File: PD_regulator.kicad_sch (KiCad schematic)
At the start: 26 parts, among them J5 Switch, J6 Fast_Out, U5 ADA4896-2ARMZ, U8 ADG1413, U9 LTC6228xS8

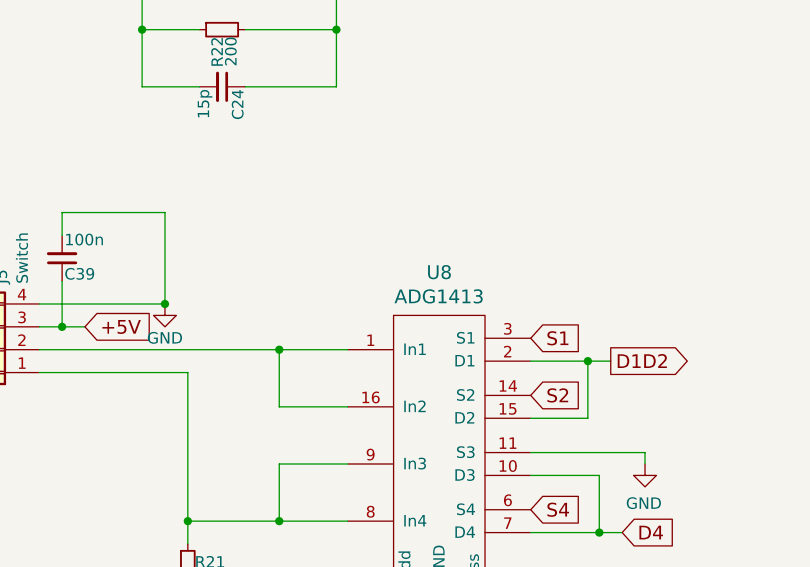
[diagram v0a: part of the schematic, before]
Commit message: Fix HMC365 and ADG1413 symbols. Update gerber files.
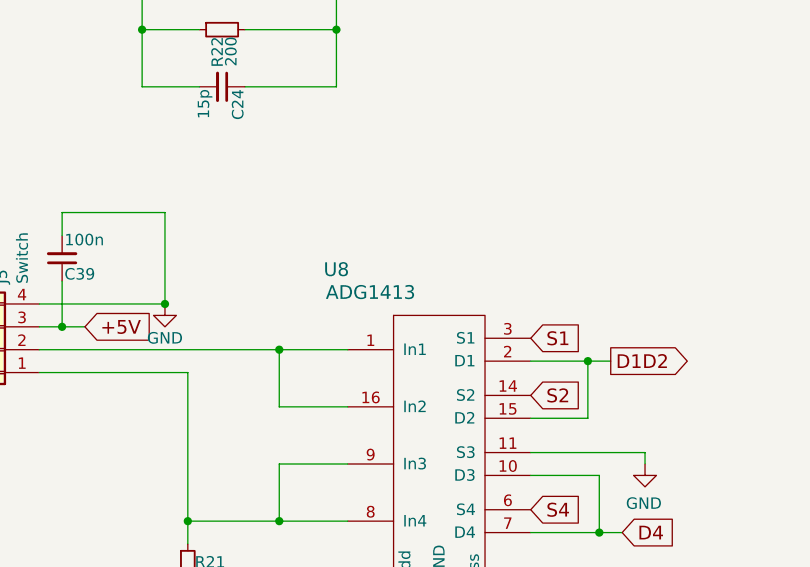
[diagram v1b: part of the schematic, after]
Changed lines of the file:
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@@
   (symbol (lib_id "Linear-Technology:ADG1413") (at 121.92 129.54 0) (unit 1)
     (in_bom yes) (on_board yes)
-    (property "Reference" "U8" (id 0) (at 121.92 104.4702 0)
+    (property "Reference" "U8" (id 0) (at 110.49 104.14 0)
       (effects (font (size 1.524 1.524)))
     )
-    (property "Value" "ADG1413" (id 1) (at 121.92 107.1626 0)
+    (property "Value" "ADG1413" (id 1) (at 114.3 106.68 0)
       (effects (font (size 1.524 1.524)))
     )
-    (property "Footprint" "Package_SO:TSSOP-16_4.4x5mm_P0.65mm" (id 2) (at 121.92 134.62 0)
+    (property "Footprint" "Package_SO:TSSOP-16_4.4x5mm_P0.65mm" (id 2) (at 154.94 142.24 0)
       (effects (font (size 1.524 1.524)) hide)
     )
@@
     (pin "10")
     (pin "11")
+    (pin "12")
     (pin "13")
     (pin "14")

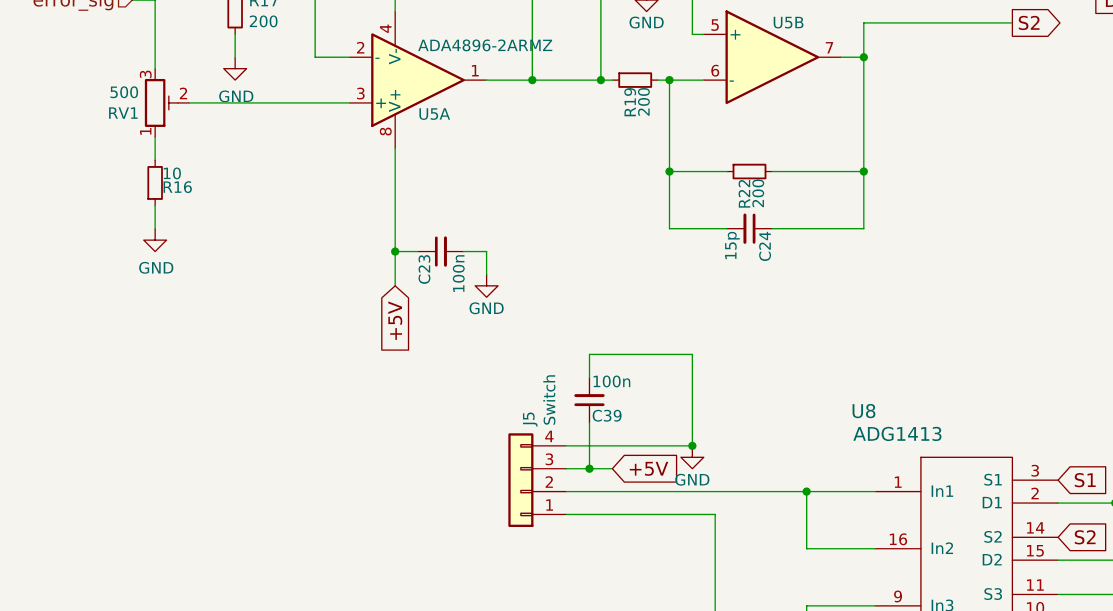
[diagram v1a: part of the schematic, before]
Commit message: Update BOM / fix some fottprints
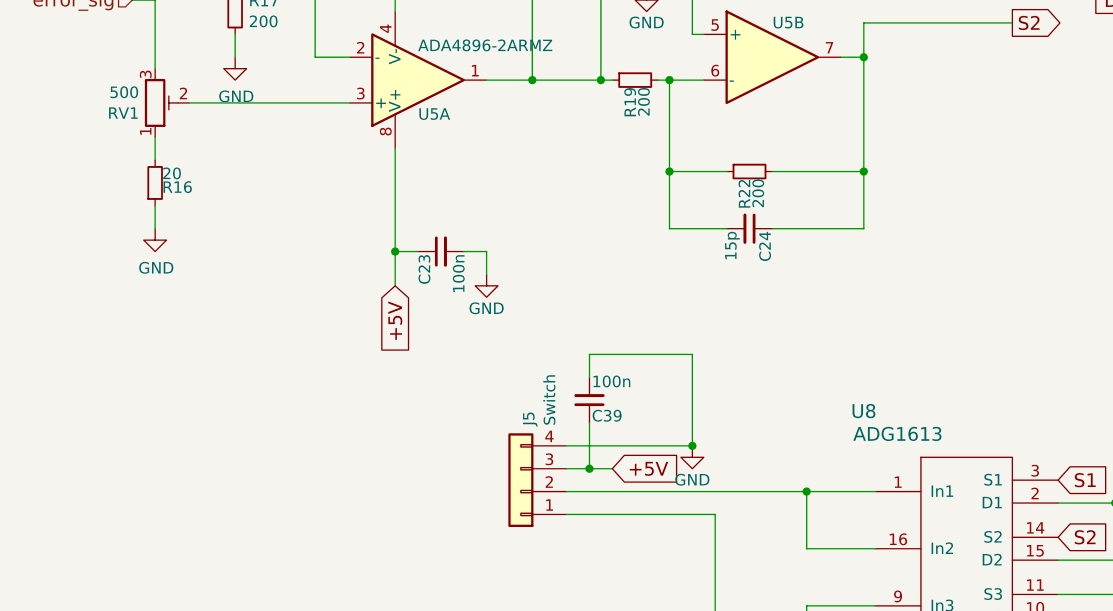
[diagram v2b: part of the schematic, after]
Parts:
- C38: Config (none) -> DNF
- R16: value 10 -> 20; MFN (none) -> Yageo; PN (none) -> AC0603FR-0720RL
- R17, R18: footprint Capacitor_SMD:C_0603_1608Metric -> Resistor_SMD:R_0603_1608Metric; MFN (none) -> Yageo; PN (none) -> RC0603FR-13200RL
- R19, R22, R23, R25: MFN (none) -> Yageo; PN (none) -> RC0603FR-13200RL
- U5: MFN (none) -> Analog Devices; PN (none) -> ADA4896-2ARMZ
- U8: value ADG1413 -> ADG1613; MFN (none) -> Analog Devices; PN (none) -> ADG1613BRUZ
- U9: MFN (none) -> Analog Devices; PN (none) -> LTC6228IS8#PBF
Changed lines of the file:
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@@
+      (effects (font (size 1.27 1.27)) hide)
+    )
+    (property "MFN" "Yageo" (id 4) (at 157.48 58.42 0)
+      (effects (font (size 1.27 1.27)) hide)
+    )
+    (property "PN" "RC0603FR-13200RL" (id 5) (at 157.48 58.42 0)
       (effects (font (size 1.27 1.27)) hide)
     )
@@
     )
     (property "Datasheet" "" (id 3) (at 191.77 26.67 0)
+      (effects (font (size 1.27 1.27)) hide)
+    )
+    (property "MFN" "Yageo" (id 4) (at 191.77 26.67 0)
+      (effects (font (size 1.27 1.27)) hide)
+    )
+    (property "PN" "RC0603FR-13200RL" (id 5) (at 191.77 26.67 0)
       (effects (font (size 1.27 1.27)) hide)
     )
@@
     (property "Datasheet" "https://www.analog.com/media/en/technical-documentation/data-sheets/LTC6228-6229.pdf" (id 3) (at 194.31 60.96 0)
       (effects (font (size 1.27 1.27)) hide)
+    )
+    (property "MFN" "Analog Devices" (id 4) (at 194.31 60.96 0)
+      (effects (font (size 1.524 1.524)) hide)
+    )
+    (property "PN" "LTC6228IS8#PBF" (id 5) (at 194.31 60.96 0)
+      (effects (font (size 1.524 1.524)) hide)
     )
     (pin "1")
@@
       (effects (font (size 1.524 1.524)))
     )
-    (property "Value" "ADG1413" (id 1) (at 114.3 106.68 0)
+    (property "Value" "ADG1613" (id 1) (at 114.3 106.68 0)
       (effects (font (size 1.524 1.524)))
     )
@@
     )
     (property "Datasheet" "" (id 3) (at 121.92 134.62 0)
+      (effects (font (size 1.524 1.524)) hide)
+    )
+    (property "MFN" "Analog Devices" (id 4) (at 121.92 129.54 0)
+      (effects (font (size 1.524 1.524)) hide)
+    )
+    (property "PN" "ADG1613BRUZ" (id 5) (at 121.92 129.54 0)
       (effects (font (size 1.524 1.524)) hide)
     )
@@
       (effects (font (size 1.27 1.27)) (justify left))
     )
-    (property "Footprint" "Capacitor_SMD:C_0603_1608Metric" (id 2) (at 40.64 59.69 0)
+    (property "Footprint" "Resistor_SMD:R_0603_1608Metric" (id 2) (at 40.64 59.69 0)
       (effects (font (size 1.27 1.27)) hide)
     )
     (property "Datasheet" "~" (id 3) (at 40.64 59.69 0)
+      (effects (font (size 1.27 1.27)) hide)
+    )
+    (property "MFN" "Yageo" (id 4) (at 40.64 59.69 0)
+      (effects (font (size 1.27 1.27)) hide)
+    )
+    (property "PN" "RC0603FR-13200RL" (id 5) (at 40.64 59.69 0)
       (effects (font (size 1.27 1.27)) hide)
     )
@@
     (property "Reference" "R18" (id 0) (at 64.77 49.6316 90))
     (property "Value" "200" (id 1) (at 64.77 51.943 90))
-    (property "Footprint" "Capacitor_SMD:C_0603_1608Metric" (id 2) (at 64.77 54.61 0)
+    (property "Footprint" "Resistor_SMD:R_0603_1608Metric" (id 2) (at 64.77 54.61 0)
       (effects (font (size 1.27 1.27)) hide)
     )
     (property "Datasheet" "~" (id 3) (at 64.77 54.61 0)
+      (effects (font (size 1.27 1.27)) hide)
+    )
+    (property "MFN" "Yageo" (id 4) (at 64.77 54.61 0)
+      (effects (font (size 1.27 1.27)) hide)
+    )
+    (property "PN" "RC0603FR-13200RL" (id 5) (at 64.77 54.61 0)
       (effects (font (size 1.27 1.27)) hide)
     )
@@
       (effects (font (size 1.27 1.27)) hide)
     )
+    (property "MFN" "Yageo" (id 4) (at 85.09 67.31 0)
+      (effects (font (size 1.27 1.27)) hide)
+    )
+    (property "PN" "RC0603FR-13200RL" (id 5) (at 85.09 67.31 0)
+      (effects (font (size 1.27 1.27)) hide)
+    )
     (pin "1")
     (pin "2")
@@
     )
     (property "Datasheet" "" (id 3) (at 97.79 77.47 0)
+      (effects (font (size 1.27 1.27)) hide)
+    )
+    (property "MFN" "Yageo" (id 4) (at 97.79 77.47 0)
+      (effects (font (size 1.27 1.27)) hide)
+    )
+    (property "PN" "RC0603FR-13200RL" (id 5) (at 97.79 77.47 0)
       (effects (font (size 1.27 1.27)) hide)
     )
@@
       (effects (font (size 1.27 1.27)) hide)
     )
+    (property "Config" "DNF" (id 4) (at 240.03 66.04 0)
+      (effects (font (size 1.27 1.27)) hide)
+    )
     (pin "1")
     (pin "2")
@@
     (property "Datasheet" "" (id 3) (at 100.33 60.96 0)
       (effects (font (size 1.27 1.27)) hide)
+    )
+    (property "MFN" "Analog Devices" (id 4) (at 100.33 64.77 0)
+      (effects (font (size 1.524 1.524)) hide)
+    )
+    (property "PN" "ADA4896-2ARMZ" (id 5) (at 100.33 64.77 0)
+      (effects (font (size 1.524 1.524)) hide)
     )
     (pin "5")
@@
       (effects (font (size 1.27 1.27)) hide)
     )
+    (property "MFN" "Analog Devices" (id 4) (at 60.96 67.31 0)
+      (effects (font (size 1.524 1.524)) hide)
+    )
+    (property "PN" "ADA4896-2ARMZ" (id 5) (at 60.96 67.31 0)
+      (effects (font (size 1.524 1.524)) hide)
+    )
     (pin "1")
     (pin "2")
@@
       (effects (font (size 1.27 1.27)) (justify left))
     )
-    (property "Value" "10" (id 1) (at 32.512 77.724 0)
+    (property "Value" "20" (id 1) (at 32.512 77.724 0)
       (effects (font (size 1.27 1.27)) (justify left))
     )
@@
       (effects (font (size 1.27 1.27)) hide)
     )
+    (property "MFN" "Yageo" (id 4) (at 31.75 78.74 0)
+      (effects (font (size 1.27 1.27)) hide)
+    )
+    (property "PN" "AC0603FR-0720RL" (id 5) (at 31.75 78.74 0)
+      (effects (font (size 1.27 1.27)) hide)
+    )

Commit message: Updated BOM with new parts
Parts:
- C22, C23, C33, C34, C36, C37, C39: MFN (none) -> KEMET; PN (none) -> C0603C104K5RAC3121
- C24: MFN (none) -> Vishay / Vitramon; PN (none) -> VJ0603A150JXBAC
- C35: MFN (none) -> KEMET; PN (none) -> C0603X102K4RACAUTO
- J6: MFN (none) -> Linx Technologies; PN (none) -> CONREVSMA006.062-G
- R21: MFN (none) -> Panasonic; PN (none) -> ERJ-3GEYJ103V
- R24: MFN (none) -> ROHM Semiconductor; PN (none) -> SDR03EZPF4R70
- R26: MFN (none) -> Vishay / Dale; PN (none) -> CRCW121049R9FKEA
- RV1: MFN (none) -> Vishay / Spectrol; PN (none) -> M43P501KB40
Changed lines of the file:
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@@
+      (effects (font (size 1.27 1.27)) hide)
+    )
+    (property "MFN" "KEMET" (id 4) (at 153.67 66.04 0)
+      (effects (font (size 1.27 1.27)) hide)
+    )
+    (property "PN" "C0603X102K4RACAUTO " (id 5) (at 153.67 66.04 0)
       (effects (font (size 1.27 1.27)) hide)
     )
@@
     )
     (property "Datasheet" "" (id 3) (at 162.56 66.04 0)
+      (effects (font (size 1.27 1.27)) hide)
+    )
+    (property "MFN" "ROHM Semiconductor " (id 4) (at 162.56 66.04 0)
+      (effects (font (size 1.27 1.27)) hide)
+    )
+    (property "PN" "SDR03EZPF4R70" (id 5) (at 162.56 66.04 0)
       (effects (font (size 1.27 1.27)) hide)
     )
@@
       (effects (font (size 1.27 1.27)) hide)
     )
+    (property "MFN" "KEMET" (id 4) (at 196.85 72.39 0)
+      (effects (font (size 1.27 1.27)) hide)
+    )
+    (property "PN" "C0603C104K5RAC3121 " (id 5) (at 196.85 72.39 0)
+      (effects (font (size 1.27 1.27)) hide)
+    )
     (pin "1")
     (pin "2")
@@
       (effects (font (size 1.27 1.27)) hide)
     )
+    (property "MFN" "KEMET" (id 4) (at 186.69 46.99 0)
+      (effects (font (size 1.27 1.27)) hide)
+    )
+    (property "PN" "C0603C104K5RAC3121 " (id 5) (at 186.69 46.99 0)
+      (effects (font (size 1.27 1.27)) hide)
+    )
     (pin "1")
     (pin "2")
@@
     )
     (property "Datasheet" "" (id 3) (at 80.01 102.87 0)
+      (effects (font (size 1.27 1.27)) hide)
+    )
+    (property "MFN" "KEMET" (id 4) (at 80.01 102.87 0)
+      (effects (font (size 1.27 1.27)) hide)
+    )
+    (property "PN" "C0603C104K5RAC3121 " (id 5) (at 80.01 102.87 0)
       (effects (font (size 1.27 1.27)) hide)
     )
@@
     )
     (property "Datasheet" "" (id 3) (at 93.98 137.16 0)
+      (effects (font (size 1.27 1.27)) hide)
+    )
+    (property "MFN" "Panasonic" (id 4) (at 93.98 137.16 0)
+      (effects (font (size 1.27 1.27)) hide)
+    )
+    (property "PN" "ERJ-3GEYJ103V" (id 5) (at 93.98 137.16 0)
       (effects (font (size 1.27 1.27)) hide)
     )
@@
       (effects (font (size 1.27 1.27)) hide)
     )
+    (property "MFN" "KEMET" (id 4) (at 113.03 156.21 0)
+      (effects (font (size 1.27 1.27)) hide)
+    )
+    (property "PN" "C0603C104K5RAC3121 " (id 5) (at 113.03 156.21 0)
+      (effects (font (size 1.27 1.27)) hide)
+    )
     (pin "1")
     (pin "2")
@@
     )
     (property "Datasheet" "" (id 3) (at 130.81 156.21 0)
+      (effects (font (size 1.27 1.27)) hide)
+    )
+    (property "MFN" "KEMET" (id 4) (at 130.81 156.21 0)
+      (effects (font (size 1.27 1.27)) hide)
+    )
+    (property "PN" "C0603C104K5RAC3121 " (id 5) (at 130.81 156.21 0)
       (effects (font (size 1.27 1.27)) hide)
     )
@@
       (effects (font (size 1.27 1.27)) hide)
     )
+    (property "MFN" "Vishay / Vitramon " (id 4) (at 97.79 83.82 0)
+      (effects (font (size 1.27 1.27)) hide)
+    )
+    (property "PN" "VJ0603A150JXBAC " (id 5) (at 97.79 83.82 0)
+      (effects (font (size 1.27 1.27)) hide)
+    )
     (pin "1")
     (pin "2")
@@
       (effects (font (size 1.524 1.524)) hide)
     )
+    (pin "1")
+    (pin "2")
+    (pin "3")
+    (pin "4")
+    (pin "8")
     (pin "5")
     (pin "6")
@@
       (effects (font (size 1.27 1.27)) hide)
     )
+    (property "MFN" "Vishay / Dale " (id 4) (at 226.06 60.96 0)
+      (effects (font (size 1.27 1.27)) hide)
+    )
+    (property "PN" "CRCW121049R9FKEA " (id 5) (at 226.06 60.96 0)
+      (effects (font (size 1.27 1.27)) hide)
+    )
     (pin "1")
     (pin "2")
@@
     (pin "4")
     (pin "8")
+    (pin "5")
+    (pin "6")
+    (pin "7")
   )
   (symbol (lib_id "power:GND") (at 247.65 66.04 0) (unit 1)
@@
       (effects (font (size 1.27 1.27)) hide)
     )
+    (property "MFN" "Linx Technologies " (id 4) (at 247.65 60.96 0)
+      (effects (font (size 1.27 1.27)) hide)
+    )
+    (property "PN" "CONREVSMA006.062-G " (id 5) (at 247.65 60.96 0)
+      (effects (font (size 1.27 1.27)) hide)
+    )
     (pin "1")
     (pin "2")
@@
       (effects (font (size 1.27 1.27)) hide)
     )
+    (property "MFN" "KEMET" (id 4) (at 63.5 86.36 0)
+      (effects (font (size 1.27 1.27)) hide)
+    )
+    (property "PN" "C0603C104K5RAC3121 " (id 5) (at 63.5 86.36 0)
+      (effects (font (size 1.27 1.27)) hide)
+    )
     (pin "1")
     (pin "2")
@@
       (effects (font (size 1.27 1.27)) hide)
     )
+    (property "MFN" "KEMET" (id 4) (at 53.34 43.18 0)
+      (effects (font (size 1.27 1.27)) hide)
+    )
+    (property "PN" "C0603C104K5RAC3121 " (id 5) (at 53.34 43.18 0)
+      (effects (font (size 1.27 1.27)) hide)
+    )
     (pin "1")
     (pin "2")
@@
       (effects (font (size 1.27 1.27)) hide)
     )
+    (property "MFN" "Vishay / Spectrol " (id 4) (at 31.75 69.85 0)
+      (effects (font (size 1.27 1.27)) hide)
+    )
+    (property "PN" "M43P501KB40 " (id 5) (at 31.75 69.85 0)
+      (effects (font (size 1.27 1.27)) hide)
+    )

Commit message: Update BOM
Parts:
- J5: MFN (none) -> JST; PN (none) -> B4B-PH-K-S
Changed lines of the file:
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@@
+      (effects (font (size 1.27 1.27)) hide)
+    )
+    (property "MFN" "JST" (id 4) (at 72.39 113.03 0)
+      (effects (font (size 1.27 1.27)) hide)
+    )
+    (property "PN" "B4B-PH-K-S" (id 5) (at 72.39 113.03 0)
       (effects (font (size 1.27 1.27)) hide)
     )

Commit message: Remove solder paste from DNF footprints.
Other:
- title: Fast PD regulator -> Phase-Frequency Detector
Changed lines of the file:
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@@
   (paper "A4")
   (title_block
-    (title "Fast PD regulator")
-    (date "2022-01-02")
-    (rev "1.4")
+    (title "Phase-Frequency Detector")
+    (date "2023-03-22")
+    (rev "1.4.1")
     (company "Atoms-Photons-Quanta, IAP, TU Darmstadt")
     (comment 1 "Tilman Preuschoff")

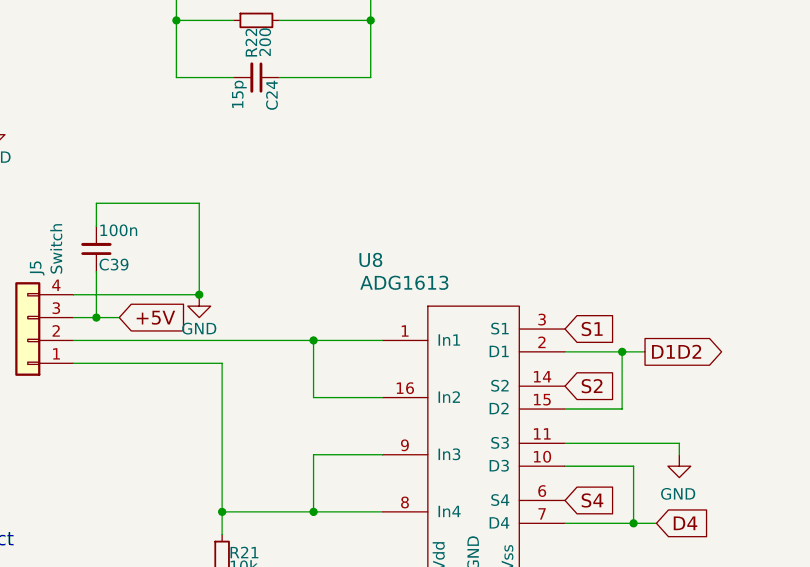
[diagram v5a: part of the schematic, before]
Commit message: Replace ADG1613 with ADG1413 due to better availability
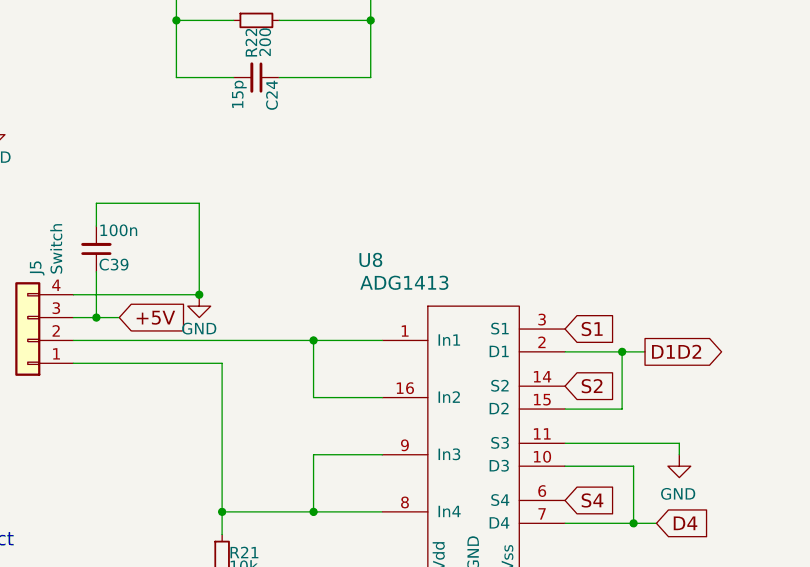
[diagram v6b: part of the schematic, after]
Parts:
- U8: value ADG1613 -> ADG1413; PN ADG1613BRUZ -> ADG1413YRUZ
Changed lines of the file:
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@@
   (title_block
     (title "Phase-Frequency Detector")
-    (date "2023-03-22")
+    (date "2023-06-16")
     (rev "1.4.1")
     (company "Atoms-Photons-Quanta, IAP, TU Darmstadt")
@@
       (effects (font (size 1.524 1.524)))
     )
-    (property "Value" "ADG1613" (id 1) (at 114.3 106.68 0)
+    (property "Value" "ADG1413" (id 1) (at 114.3 106.68 0)
       (effects (font (size 1.524 1.524)))
     )
@@
       (effects (font (size 1.524 1.524)) hide)
     )
-    (property "PN" "ADG1613BRUZ" (id 5) (at 121.92 129.54 0)
+    (property "PN" "ADG1413YRUZ" (id 5) (at 121.92 129.54 0)
       (effects (font (size 1.524 1.524)) hide)
     )

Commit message: Correct PN for Harting and BNC connectors
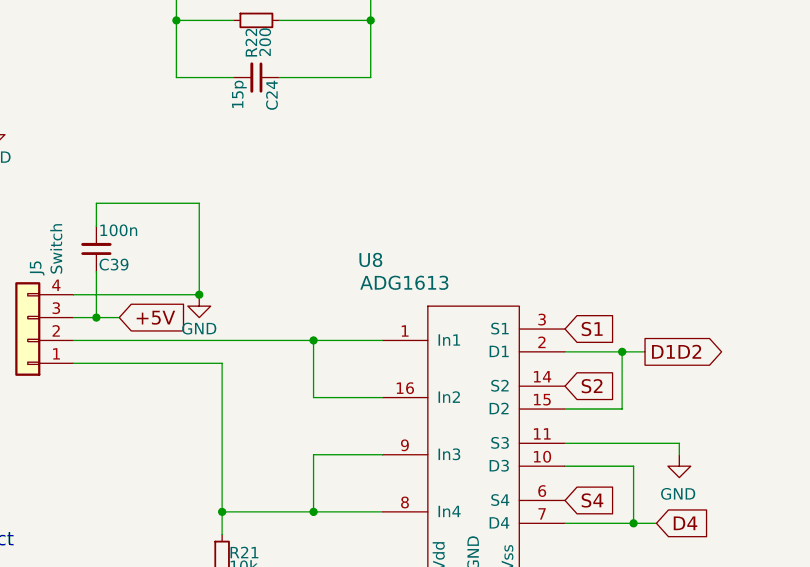
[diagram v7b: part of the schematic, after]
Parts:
- J6: PN CONREVSMA006.062-G -> CONBNC002
- U8: value ADG1413 -> ADG1613; PN ADG1413YRUZ -> ADG1613BRUZ
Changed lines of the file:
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@@
       (effects (font (size 1.524 1.524)))
     )
-    (property "Value" "ADG1413" (id 1) (at 114.3 106.68 0)
+    (property "Value" "ADG1613" (id 1) (at 114.3 106.68 0)
       (effects (font (size 1.524 1.524)))
     )
@@
       (effects (font (size 1.524 1.524)) hide)
     )
-    (property "PN" "ADG1413YRUZ" (id 5) (at 121.92 129.54 0)
+    (property "PN" "ADG1613BRUZ" (id 5) (at 121.92 129.54 0)
       (effects (font (size 1.524 1.524)) hide)
     )
@@
       (effects (font (size 1.27 1.27)) hide)
     )
-    (property "PN" "CONREVSMA006.062-G " (id 5) (at 247.65 60.96 0)
-      (effects (font (size 1.27 1.27)) hide)
-    )
+    (property "PN" "CONBNC002" (id 5) (at 247.65 60.96 0)
+      (effects (font (size 1.27 1.27)) hide)
+    )
